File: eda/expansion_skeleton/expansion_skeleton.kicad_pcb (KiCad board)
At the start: 2 copper layers, 182.4 x 99.1 mm, 12 parts, among them J2 Bus expansion

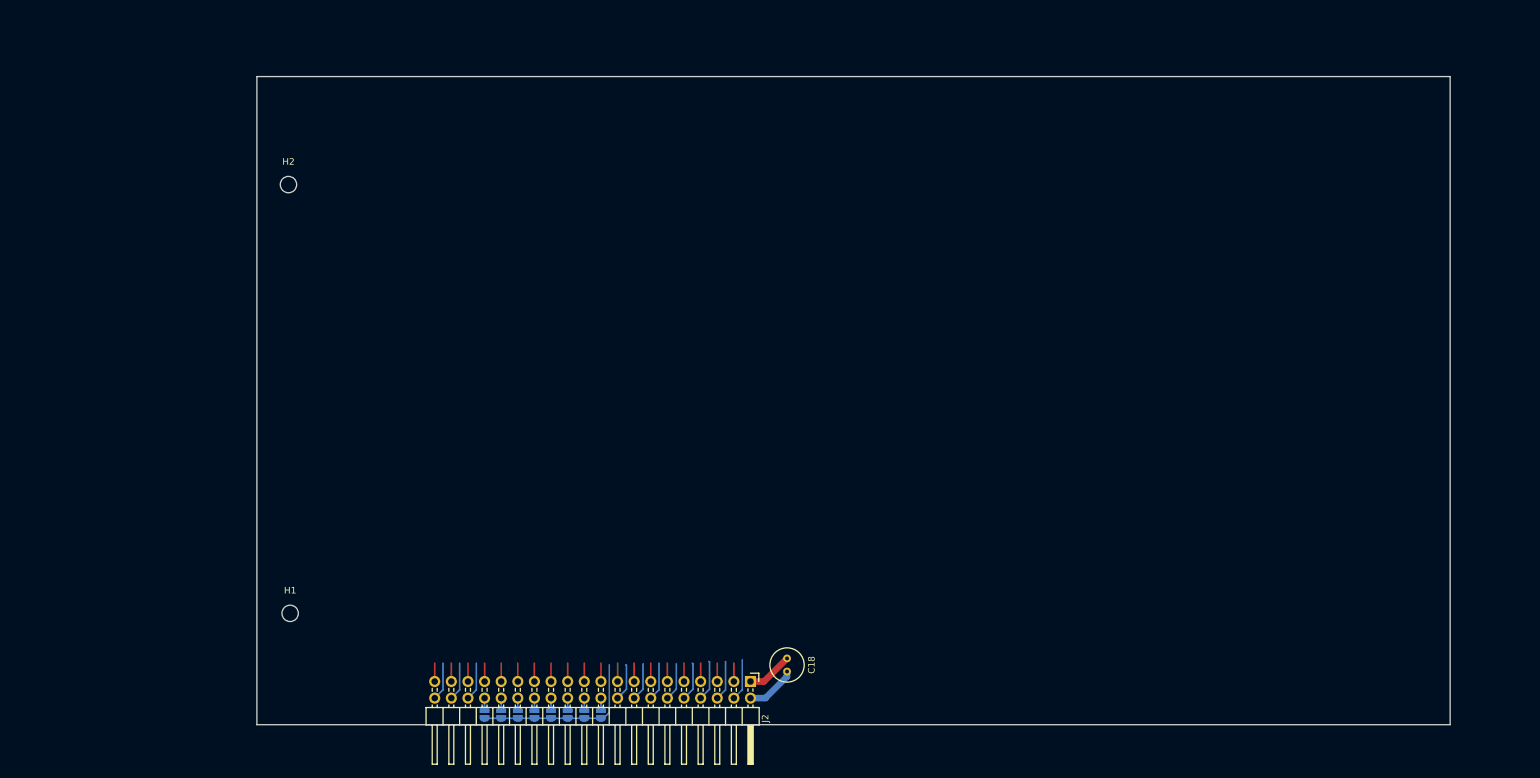
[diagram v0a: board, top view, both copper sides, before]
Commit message: EDA work for new expansion header
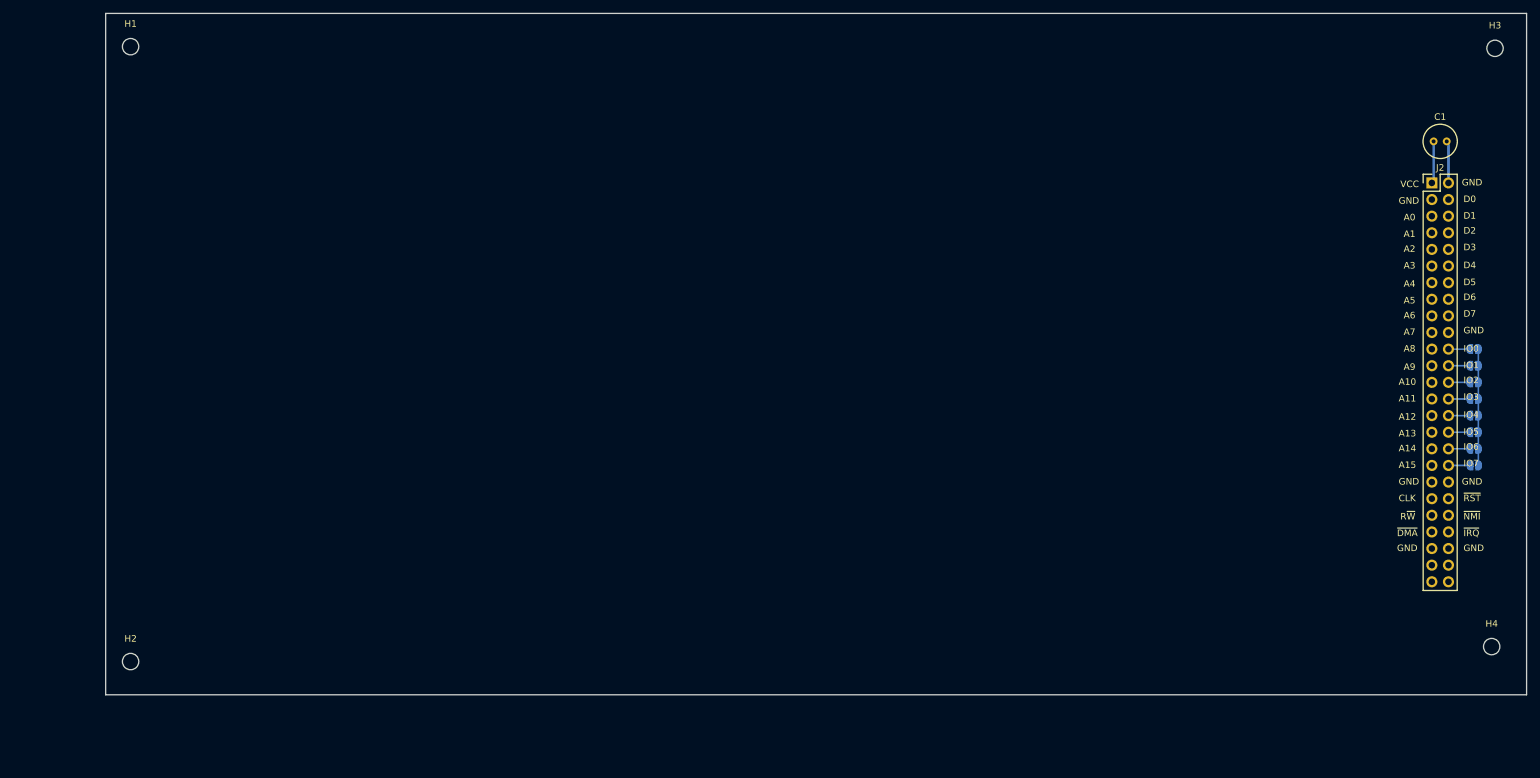
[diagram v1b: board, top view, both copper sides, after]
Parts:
- removed C18: 100nf, Capacitor_THT:C_Radial_D5.0mm_H7.0mm_P2.00mm
- removed JP1, JP2, JP3, JP4, JP5, JP6, JP7, JP8: SolderJumper_2_Open, Jumper:SolderJumper-2_P1.3mm_Open_RoundedPad1.0x1.5mm
- added C1: 100nf, Capacitor_THT:C_Radial_D5.0mm_H7.0mm_P2.00mm, F.Cu at (232.7, 39.6)
- added H3: Standoffs, MountingHole:MountingHole_2.5mm, F.Cu at (242.1, 25.4)
- added H4: Standoffs, MountingHole:MountingHole_2.5mm, F.Cu at (241.6, 116.8)
- added JP10: SolderJumper_2_Open, Jumper:SolderJumper-2_P1.3mm_Open_RoundedPad1.0x1.5mm, B.Cu at (238.9, 73.9)
- added JP11: SolderJumper_2_Open, Jumper:SolderJumper-2_P1.3mm_Open_RoundedPad1.0x1.5mm, B.Cu at (238.9, 76.5)
- added JP12: SolderJumper_2_Open, Jumper:SolderJumper-2_P1.3mm_Open_RoundedPad1.0x1.5mm, B.Cu at (238.9, 79.0)
- added JP13: SolderJumper_2_Open, Jumper:SolderJumper-2_P1.3mm_Open_RoundedPad1.0x1.5mm, B.Cu at (238.9, 81.5)
- added JP14: SolderJumper_2_Open, Jumper:SolderJumper-2_P1.3mm_Open_RoundedPad1.0x1.5mm, B.Cu at (238.9, 84.1)
- added JP15: SolderJumper_2_Open, Jumper:SolderJumper-2_P1.3mm_Open_RoundedPad1.0x1.5mm, B.Cu at (238.9, 86.6)
- added JP16: SolderJumper_2_Open, Jumper:SolderJumper-2_P1.3mm_Open_RoundedPad1.0x1.5mm, B.Cu at (238.9, 89.2)
- added JP9: SolderJumper_2_Open, Jumper:SolderJumper-2_P1.3mm_Open_RoundedPad1.0x1.5mm, B.Cu at (238.9, 71.4)
- H1, H2: value Bracket mounting -> Standoffs
- J2: value Bus expansion -> Expansion; footprint Connector_PinHeader_2.54mm:PinHeader_2x20_P2.54mm_Horizontal -> Connector_PinHeader_2.54mm:PinHeader_2x25_P2.54mm_Vertical
- moved J2 129.0 mm to (232.4, 46.0), turned to 0 degrees
- moved H1 90.0 mm to (33.5, 25.1)
- moved H2 76.8 mm to (33.5, 119.1)
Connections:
- J2 pad 11: /Expansion/A4 -> /Expansion/A3
- J2 pad 13: /Expansion/A5 -> /Expansion/A4
- J2 pad 15: /Expansion/A6 -> /Expansion/A5
- J2 pad 17: /Expansion/A7 -> /Expansion/A6
- J2 pad 19: /Expansion/A8 -> /Expansion/A7
- J2 pad 20: Net-(J2-Pin_20) -> /Expansion/GND
- J2 pad 21: /Expansion/A9 -> /Expansion/A8
- J2 pad 23: /Expansion/A10 -> /Expansion/A9
- J2 pad 25: /Expansion/A11 -> /Expansion/A10
- J2 pad 27: /Expansion/A12 -> /Expansion/A11
- J2 pad 29: /Expansion/A13 -> /Expansion/A12
- J2 pad 3: /Expansion/A0 -> /Expansion/GND
- J2 pad 31: /Expansion/A14 -> /Expansion/A13
- J2 pad 33: /Expansion/A15 -> /Expansion/A14
- J2 pad 35: /Expansion/Clock -> /Expansion/A15
- J2 pad 36: /Expansion/~{RST} -> Net-(J2-Pin_36)
- J2 pad 37: /Expansion/R~{W} -> /Expansion/GND
- J2 pad 38: /Expansion/~{NMI} -> /Expansion/GND
- J2 pad 39: /Expansion/~{DMA} -> /Expansion/Clock
- J2 pad 40: /Expansion/~{IRQ} -> /Expansion/~{RST}
- J2 pad 5: /Expansion/A1 -> /Expansion/A0
- J2 pad 7: /Expansion/A2 -> /Expansion/A1
- J2 pad 9: /Expansion/A3 -> /Expansion/A2
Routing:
- net /Expansion/~{CS}: track 26.7 -> 17.8 mm
- net /Expansion/D0: track 6.37 -> 0.00 mm
- net /Expansion/D2: track 6.19 -> 0.00 mm
- net /Expansion/D1: track 6.11 -> 0.00 mm
- net /Expansion/D3: track 5.94 -> 0.00 mm
- net /Expansion/~{RST}: track 5.86 -> 0.00 mm
- net /Expansion/~{NMI}: track 5.86 -> 0.00 mm
- net /Expansion/~{IRQ}: track 5.86 -> 0.00 mm
- net /Expansion/D5: track 5.86 -> 0.00 mm
- net /Expansion/D6: track 5.80 -> 0.00 mm
- net /Expansion/D4: track 5.80 -> 0.00 mm
- net /Expansion/D7: track 5.68 -> 0.00 mm
- net Net-(J2-Pin_36): track 0.00 -> 3.30 mm
- net /Expansion/~{DMA}: track 2.79 -> 0.00 mm
- net /Expansion/R~{W}: track 2.79 -> 0.00 mm
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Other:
- board size 182.4 x 99.1 mm -> 217.2 x 104.1 mm
- board text added: "A0"
- board text added: "A1"
- board text added: "A10"
- board text added: "A11"
- board text added: "A12"
- board text added: "A13"
- board text added: "A14"
- board text added: "A15"
- board text added: "A2"
- board text added: "A3"
- board text added: "A4"
- board text added: "A5"
- board text added: "A6"
- board text added: "A7"
- board text added: "A8"
- board text added: "A9"
- board text added: "CLK"
- board text added: "D0"
- board text added: "D1"
- board text added: "D2"
- board text added: "D3"
- board text added: "D4"
- board text added: "D5"
- board text added: "D6"
- board text added: "D7"
- board text added: "GND"
- board text added: "IO0"
- board text added: "IO1"
- board text added: "IO2"
- board text added: "IO3"
- board text added: "IO4"
- board text added: "IO5"
- board text added: "IO6"
- board text added: "IO7"
- board text added: "R~{W}"
- board text added: "VCC"
- board text added: "~{DMA}"
- board text added: "~{IRQ}"
- board text added: "~{NMI}"
- board text added: "~{RST}"

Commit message: Branch of uart to v1
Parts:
- added H5: MountingHole_Pad, MountingHole:MountingHole_2.5mm_Pad_Via, F.Cu at (150.2, 26.0)
- added H6: MountingHole_Pad, MountingHole:MountingHole_2.5mm_Pad_Via, F.Cu at (150.4, 116.9)
- H1, H2, H3, H4: value Standoffs -> MountingHole_Pad; footprint MountingHole:MountingHole_2.5mm -> MountingHole:MountingHole_2.5mm_Pad_Via
- J2: value Expansion -> Conn_02x25_Odd_Even
- moved H2 13.7 mm to (20.1, 116.8)
- moved H1 13.5 mm to (20.1, 25.9)
- moved H3 1.00 mm to (241.2, 25.9)
- moved H4 0.35 mm to (241.2, 116.8)
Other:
- board size 217.2 x 104.1 mm -> 230 x 100 mm
